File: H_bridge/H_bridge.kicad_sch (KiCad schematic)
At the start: 18 parts, among them J1 Conn_01x10_Pin, J10 Conn_Coaxial, J11 Conn_Coaxial, J12 Conn_01x04_Pin, J2 Conn_01x10_Pin, J3 Conn_01x04_Pin, J4 Conn_01x05, J5 Conn_01x03, J6 Conn_Coaxial, J7 Conn_Coaxial, J8 Conn_Coaxial, J9 Conn_Coaxial

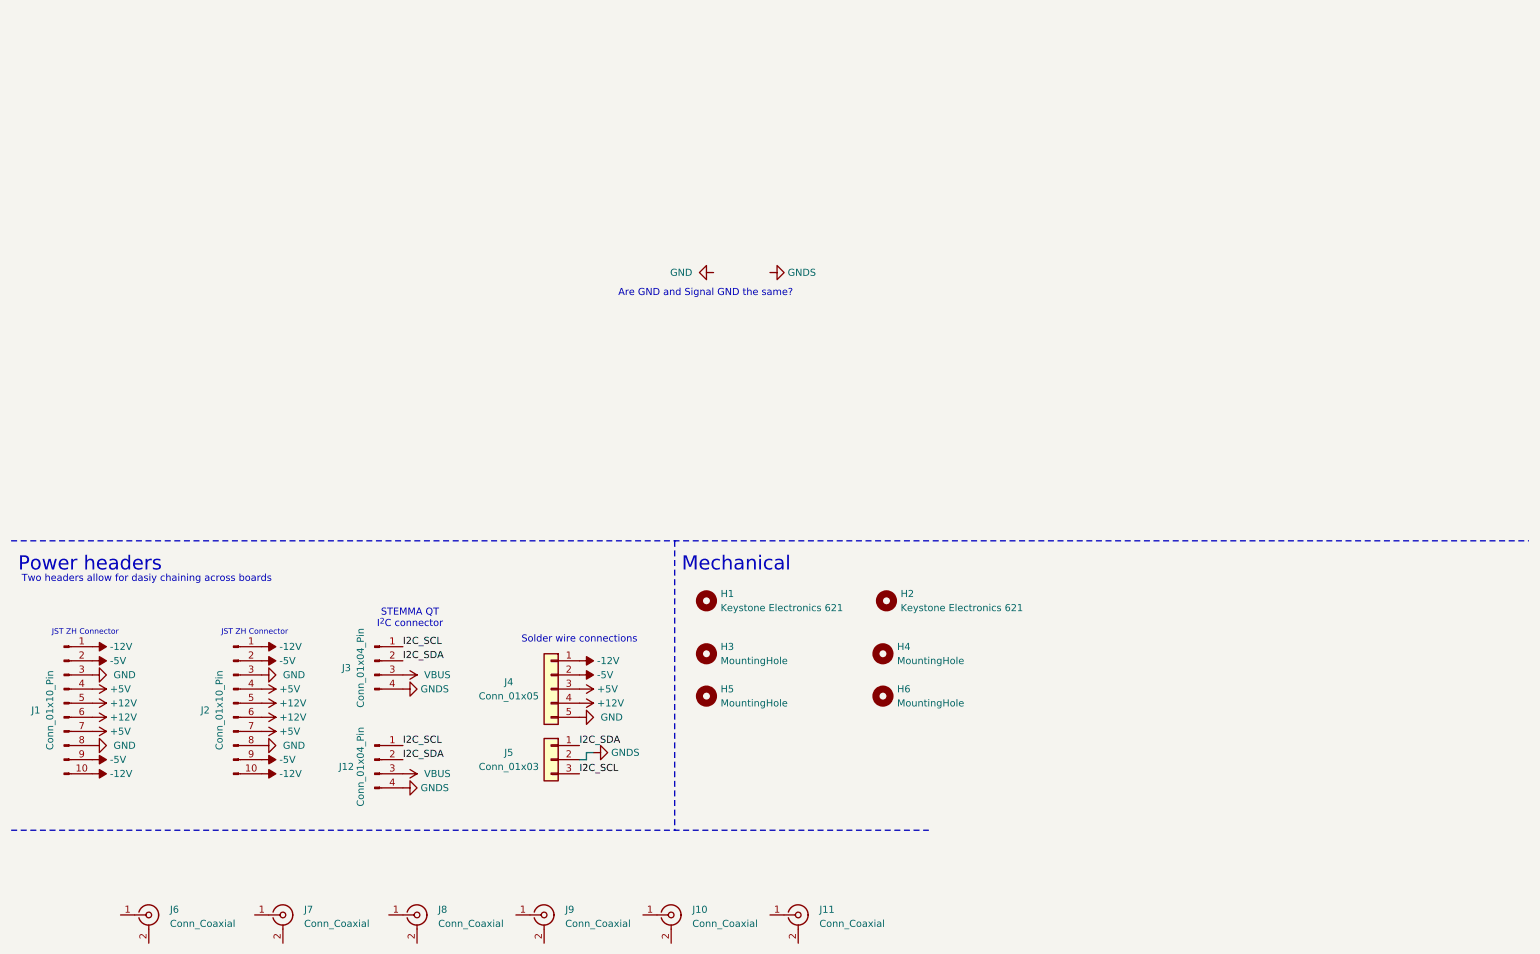
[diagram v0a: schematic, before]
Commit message: updated 3-channel H-bridge
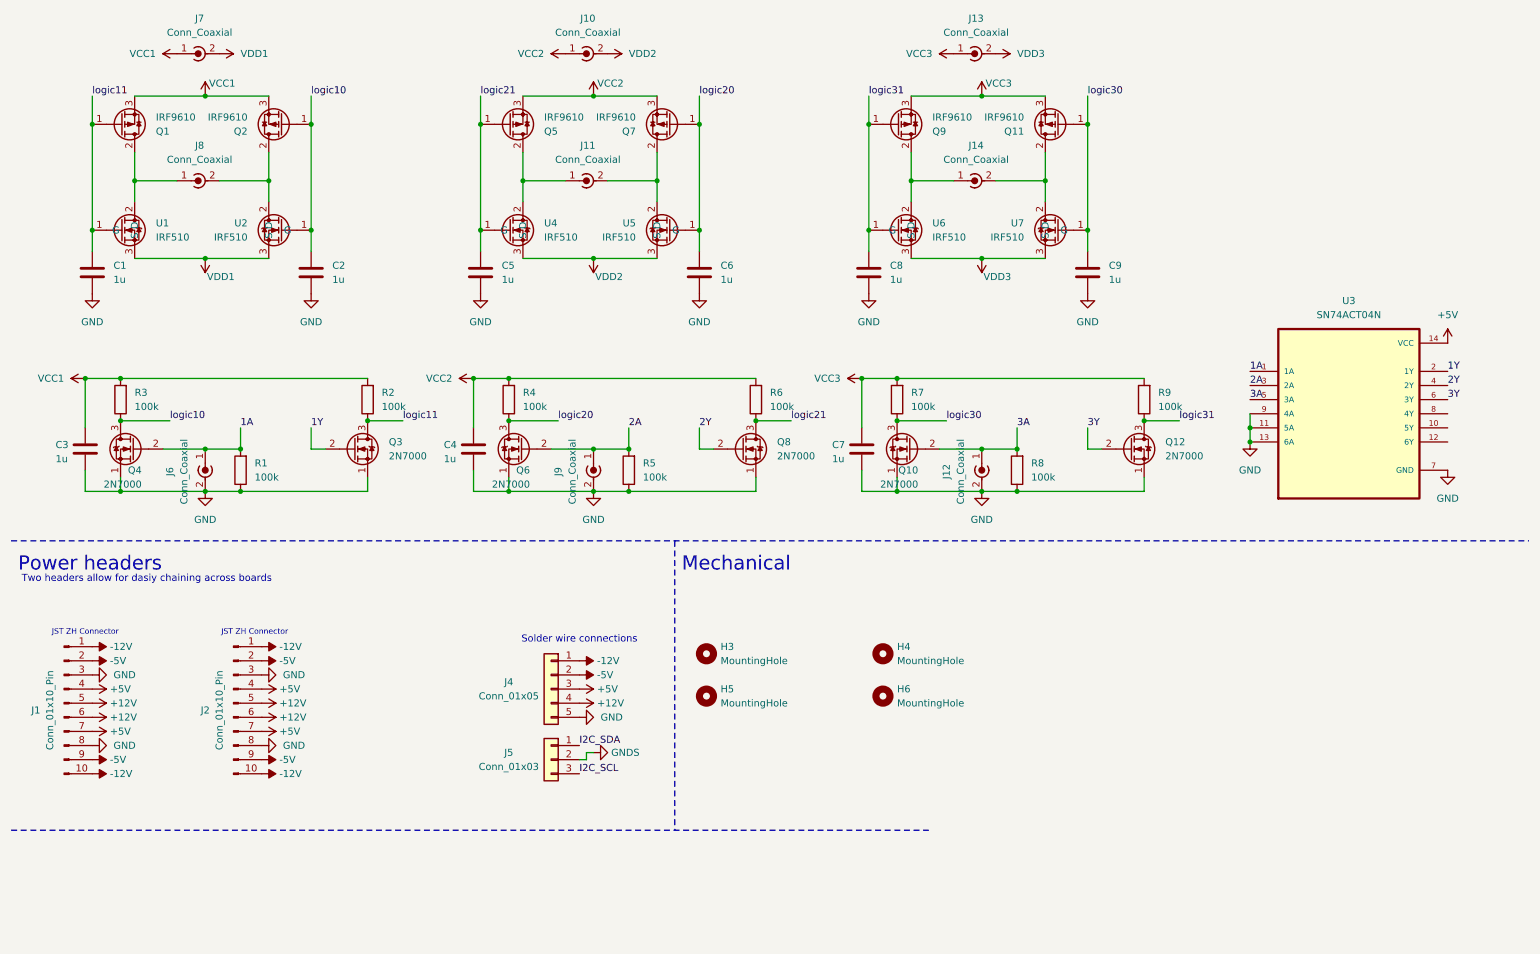
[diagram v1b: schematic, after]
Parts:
- removed H1, H2: Keystone Electronics 621, matterwaves:Keystone 621, symbol Mechanical:MountingHole
- removed J10, J11, J6, J7, J8, J9: Conn_Coaxial, Connector_Coaxial:SMA_Molex_73251-1153_EdgeMount_Horizontal, symbol Connector:Conn_Coaxial
- removed J12, J3: Conn_01x04_Pin, Connector_JST:JST_PH_S4B-PH-K_1x04_P2.00mm_Horizontal, symbol Connector:Conn_01x04_Pin
- added C1, C2, C3, C4, C5, C6, C7, C8, C9: 1u, Capacitor_THT:C_Disc_D4.3mm_W1.9mm_P5.00mm, symbol Device:C
- added J10, J11, J12, J13, J14, J6, J7, J8, J9: Conn_Coaxial, Connector_Coaxial:SMA_Molex_73251-1153_EdgeMount_Horizontal, symbol Connector:Conn_Coaxial_Power
- added Q1, Q11, Q2, Q5, Q7, Q9: IRF9610, Package_TO_SOT_THT:TO-220-3_Vertical, symbol Transistor_FET:Q_PMOS_DGS
- added Q10, Q12, Q3, Q4, Q6, Q8: 2N7000, Package_TO_SOT_THT:TO-92_Inline, symbol Transistor_FET:2N7000
- added R1, R2, R3, R4, R5, R6, R7, R8, R9: 100k, Resistor_THT:R_Axial_DIN0207_L6.3mm_D2.5mm_P10.16mm_Horizontal, symbol Device:R
- added U1, U2, U4, U5, U6, U7: IRF510, Package_TO_SOT_THT:TO-220-3_Vertical, symbol matterwaves_symbol:IRF520
- added U3: SN74ACT04N, Package_DIP:DIP-14_W7.62mm_Socket_LongPads, symbol not_gate:SN74HCT04N
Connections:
- net +5V: now also U3.14 (VCC)
- net GND: now also C1.2, C2.2, C3.2, C4.2, C5.2, C6.2, C7.2, C8.2, C9.2, J12.2 (Ext), J6.2 (Ext), J9.2 (Ext), Q10.1 (S), Q12.1 (S), Q3.1 (S), Q4.1 (S), Q6.1 (S), Q8.1 (S), R1.1, R5.1, R8.1, U3.11 (5A), U3.13 (6A), U3.7 (GND), U3.9 (4A)
- new net: J11.1 (In), Q5.2 (D), U4.2 (D)
- new net: J11.2 (Ext), Q7.2 (D), U5.2 (D)
- new net: J8.1 (In), Q1.2 (D), U1.2 (D)
- new net: J14.1 (In), Q9.2 (D), U6.2 (D)
- new net: J8.2 (Ext), Q2.2 (D), U2.2 (D)
- new net: J14.2 (Ext), Q11.2 (D), U7.2 (D)
- new net 1A: J6.1 (In), Q4.2 (G), R1.2, U3.1 (1A)
- new net 1Y: Q3.2 (G), U3.2 (1Y)
- new net 2A: J9.1 (In), Q6.2 (G), R5.2, U3.3 (2A)
- new net 2Y: Q8.2 (G), U3.4 (2Y)
- new net 3A: J12.1 (In), Q10.2 (G), R8.2, U3.5 (3A)
- new net 3Y: Q12.2 (G), U3.6 (3Y)
- new net VCC1: C3.1, J7.1 (In), Q1.3 (S), Q2.3 (S), R2.2, R3.2
- new net VCC2: C4.1, J10.1 (In), Q5.3 (S), Q7.3 (S), R4.2, R6.2
- new net VCC3: C7.1, J13.1 (In), Q11.3 (S), Q9.3 (S), R7.2, R9.2
- new net VDD1: J7.2 (Ext), U1.3 (S), U2.3 (S)
- new net VDD2: J10.2 (Ext), U4.3 (S), U5.3 (S)
- new net VDD3: J13.2 (Ext), U6.3 (S), U7.3 (S)
- new net logic10: C2.1, Q2.1 (G), Q4.3 (D), R3.1, U2.1 (G)
- new net logic11: C1.1, Q1.1 (G), Q3.3 (D), R2.1, U1.1 (G)
- new net logic20: C6.1, Q6.3 (D), Q7.1 (G), R4.1, U5.1 (G)
- new net logic21: C5.1, Q5.1 (G), Q8.3 (D), R6.1, U4.1 (G)
- new net logic30: C9.1, Q10.3 (D), Q11.1 (G), R7.1, U7.1 (G)
- new net logic31: C8.1, Q12.3 (D), Q9.1 (G), R9.1, U6.1 (G)
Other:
- note removed: "Are GND and Signal GND the same?"
- note removed: "STEMMA QT I^{2}C connector"

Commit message: generate production files for H-bridge
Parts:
- C1, C2, C3, C4, C5, C6, C7, C8, C9: LCSC (none) -> C94708
- Q1, Q11, Q2, Q5, Q7, Q9: LCSC (none) -> C335250
- Q10, Q12, Q3, Q4, Q6, Q8: LCSC (none) -> C9114
- U1, U2, U4, U5, U6, U7: LCSC (none) -> C727603
